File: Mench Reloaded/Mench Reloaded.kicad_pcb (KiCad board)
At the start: 2 copper layers, 100 x 100 mm, 55 parts, among them IC1 DS1813, J1 XBUS_265, J10 Int Sel 1, J11 VIA1 Port A, J12 VIA1 Port B, J2 TGx, J3 RAM CSB select, J4 P4x, J5 P5x, J6 P6x, J7 FTDI serial, J8 EEPROM R/W, J9 DC Power, SW1 SW_Push, U1 W65C265SxQ, U2 68c128 SRAM, U3 28C256, U4 LM1117 TO-252-3, U5 74HC00, U6 W65C22SxP, Y1 32.768 kHz, Y2 3.6864 mHz

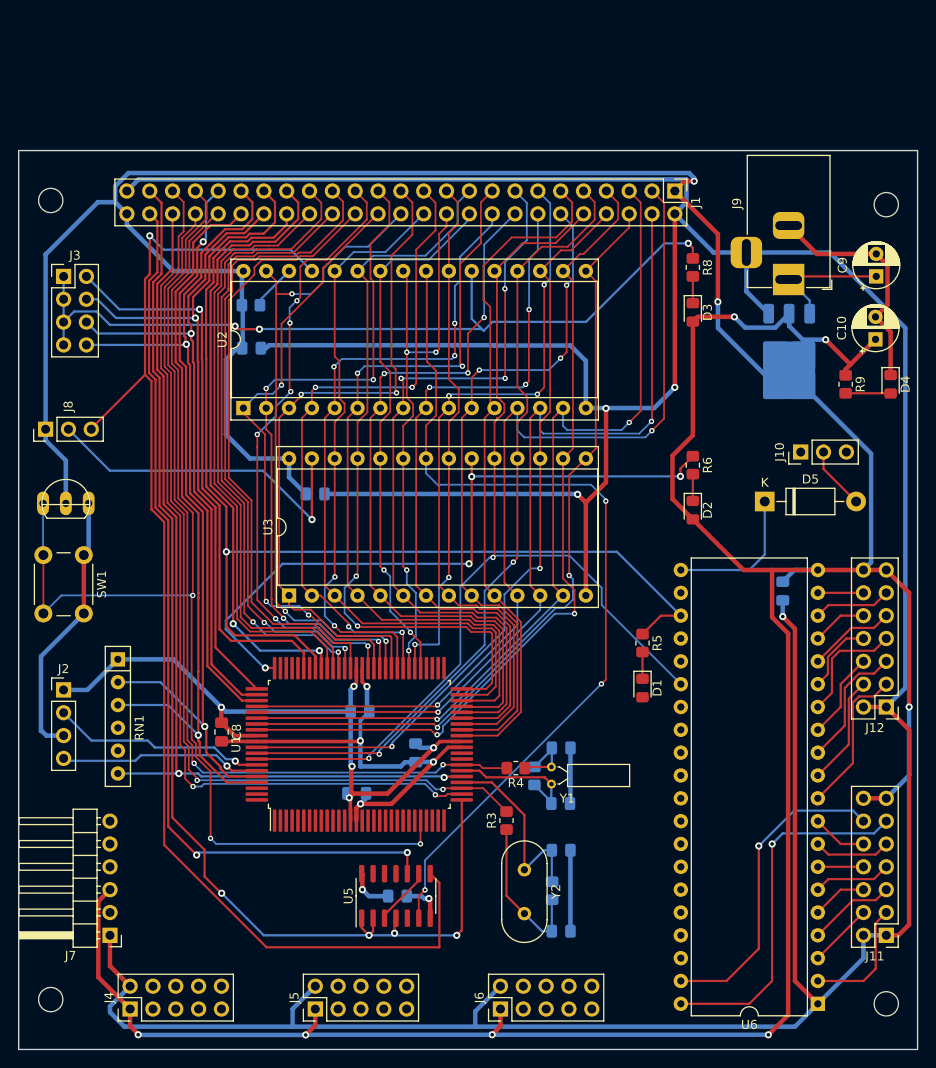
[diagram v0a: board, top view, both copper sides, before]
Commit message: Routed traces for the 65c22.
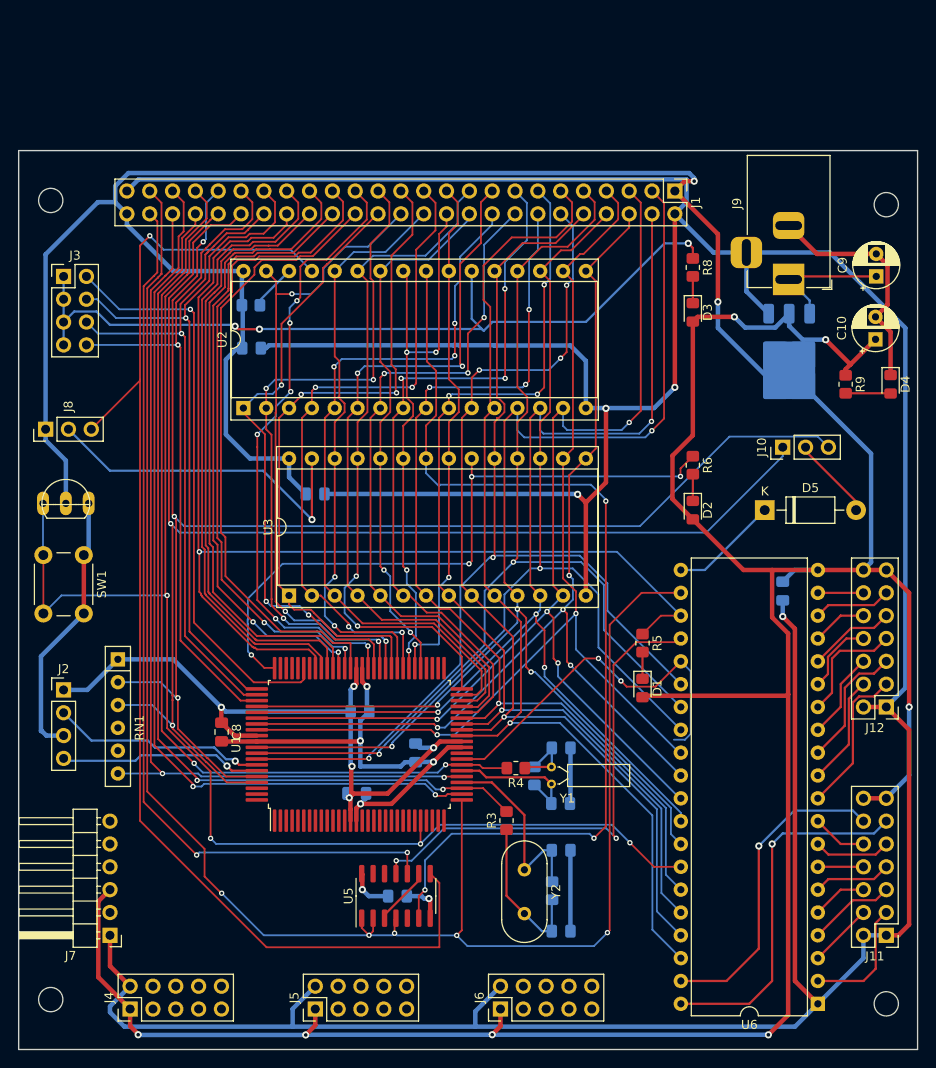
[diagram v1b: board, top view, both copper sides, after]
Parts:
- moved J10 2.07 mm to (140.0, 78.0)
- moved D5 0.96 mm to (138.0, 85.0)
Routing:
- net NMIB: track 84.0 -> 158.4 mm, vias 2 -> 3
- net IRQB: track 83.5 -> 153.9 mm, vias 1 -> 2
- net WEB: track 131.9 -> 194.0 mm, vias 4 -> 5
- net A5B: track 0.00 -> 56.0 mm, vias 0 -> 2
- net PHI2: track 100.2 -> 142.8 mm, vias 2 -> 4
- net a0: track 75.8 -> 113.1 mm, vias 0 -> 1
- net a1: track 76.3 -> 110.6 mm, vias 3 -> 4
- net d0: track 103.9 -> 137.9 mm, vias 2 -> 4
- net a2: track 81.1 -> 112.1 mm, vias 3 -> 4
- net d1: track 98.3 -> 128.0 mm, vias 2 -> 4
- net RESB: track 129.5 -> 159.0 mm, vias 3 -> 4
- net a3: track 80.1 -> 108.8 mm, vias 3 -> 4
- net d6: track 89.4 -> 117.6 mm
- net d2: track 98.3 -> 125.3 mm, vias 2 -> 4
- net d5: track 86.4 -> 113.0 mm
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
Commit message: Completed all traces. Added a Zif socket footprint to ensure one will fit. Added a solder jumper for RAM options.
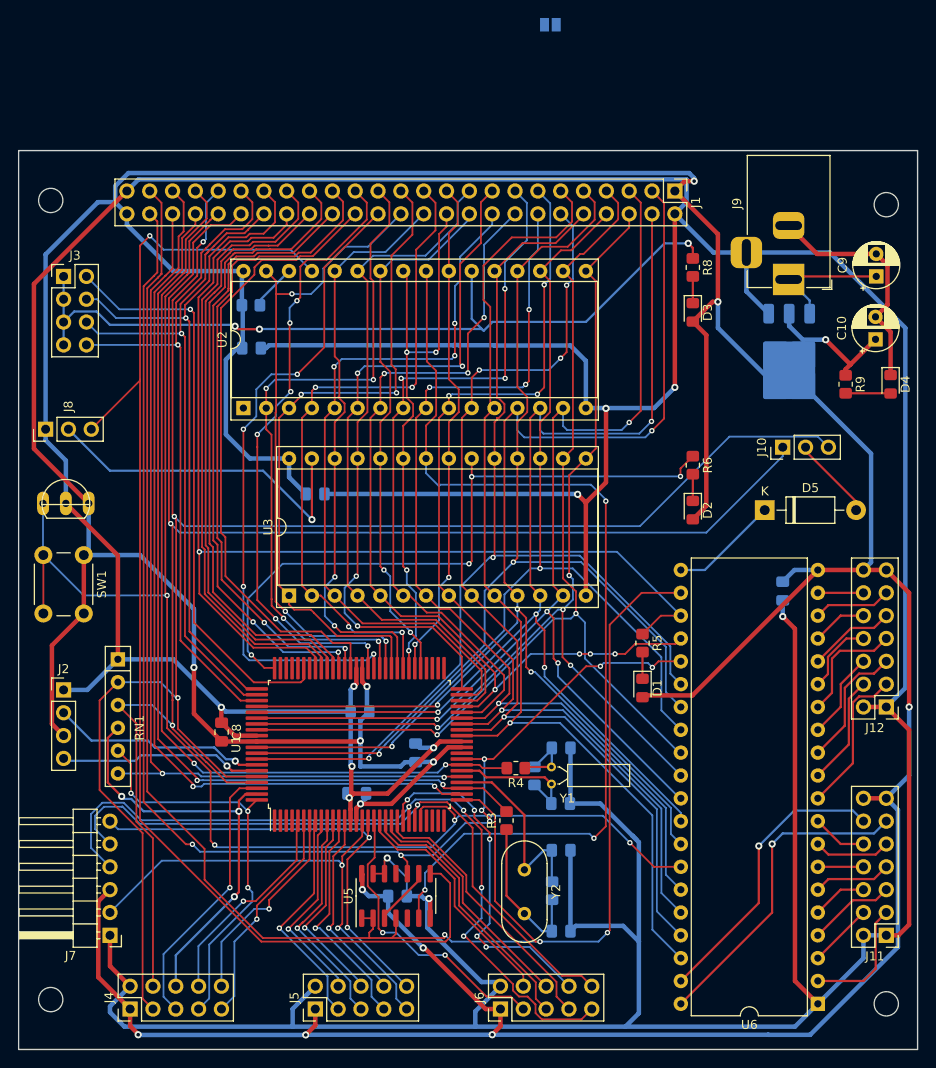
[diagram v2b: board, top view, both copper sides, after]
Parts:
- added JP1: 68c256 Jumper, Jumper:SolderJumper-2_P1.3mm_Open_Pad1.0x1.5mm, B.Cu at (114.2, 31.0)
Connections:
- U2 pad 1: a17 -> unconnected-(U2-NC-Pad1)
- U5 pad 11: A5B -> unconnected-(U5-Pad11)
- U5 pad 12: a5 -> GND
- U5 pad 13: a5 -> GND
- U6 pad 24: A5B -> a5
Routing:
- net GND: track 593.7 -> 726.1 mm, vias 9 -> 11
- net RXD3: track 0.00 -> 87.8 mm, vias 0 -> 4
- net TXD3: track 0.00 -> 75.6 mm, vias 0 -> 1
- net A5B: track 56.0 -> 0.00 mm, vias 2 -> 0
- net DTRB3: track 0.00 -> 53.9 mm, vias 0 -> 2
- net DSRB3: track 0.00 -> 51.8 mm, vias 0 -> 2
- net FA15: track 0.00 -> 48.3 mm, vias 0 -> 3
- net AMS: track 0.00 -> 45.5 mm, vias 0 -> 3
- net NMIB: track 158.4 -> 198.0 mm
- net TXD2: track 0.00 -> 39.1 mm, vias 0 -> 5
- net IRQB: track 153.9 -> 186.8 mm
- net RXD0: track 0.00 -> 32.7 mm, vias 0 -> 2
- net PIIB: track 0.00 -> 30.6 mm, vias 0 -> 1
- net RXD2: track 0.00 -> 30.6 mm
- net RXD1: track 0.00 -> 30.2 mm
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
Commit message: Added power selector header (ftdi vs battery). Added 128kB vs 256kB RAM selector. Added pull up for RESB and DS1813. Reworked traces at top of the board using streets and avenues.
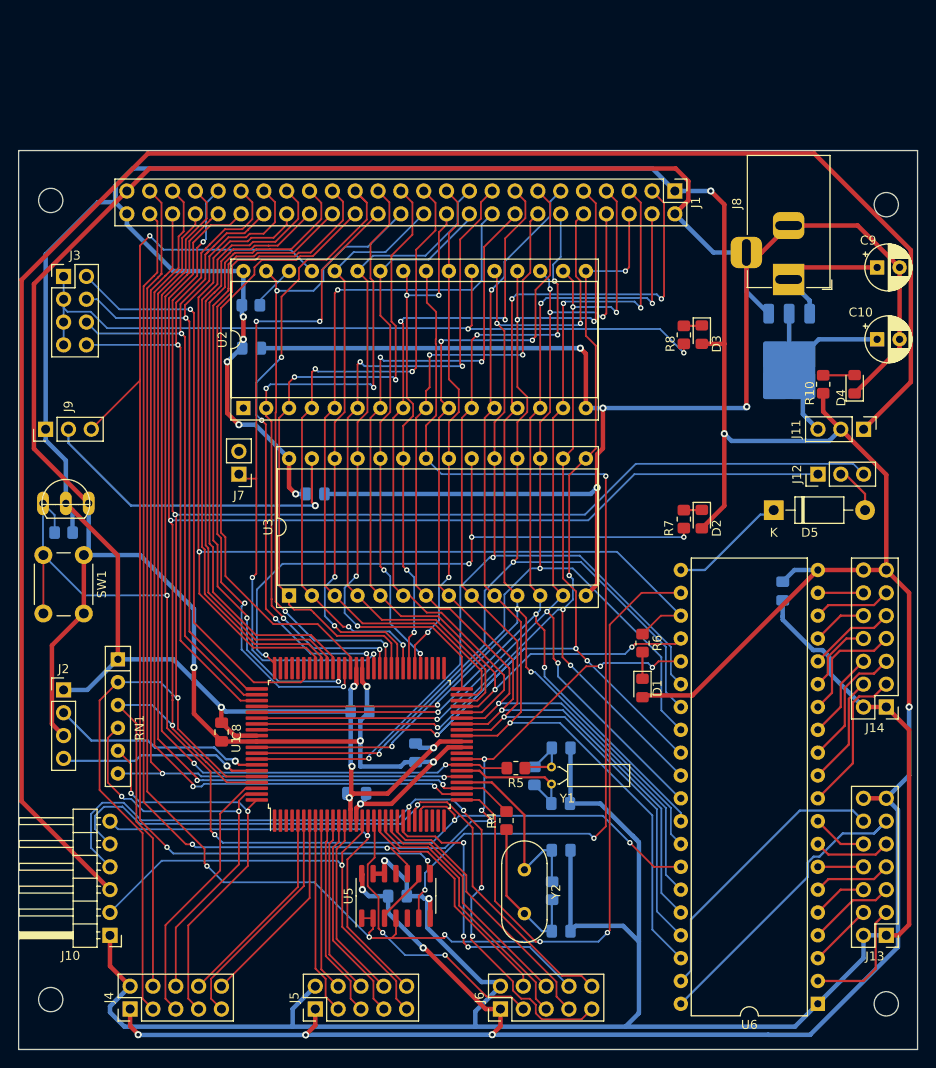
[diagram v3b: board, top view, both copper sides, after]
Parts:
- removed JP1: 68c256 Jumper, Jumper:SolderJumper-2_P1.3mm_Open_Pad1.0x1.5mm
- added J11: Power Sel, Connector_PinHeader_2.54mm:PinHeader_1x03_P2.54mm_Vertical, F.Cu at (149.0, 76.0)
- added J7: 68c256 Sel, Connector_PinHeader_2.54mm:PinHeader_1x02_P2.54mm_Vertical, F.Cu at (79.5, 81.0)
- added R1: 3K, Resistor_SMD:R_0805_2012Metric_Pad1.20x1.40mm_HandSolder, B.Cu at (60.0, 87.5)
- D1, D2, D3: value green -> LED
- J12: renamed from J10; value Int Sel 1 -> Int Sel
- moved R8 7.57 mm to (129.0, 65.5), turned to 90 degrees
- moved R7 6.08 mm to (129.0, 86.0), turned to 90 degrees
- moved J12 4.94 mm to (143.9, 81.0)
- moved D4 4.00 mm to (148.0, 71.0), turned to 90 degrees
- moved D3 2.67 mm to (131.0, 65.5)
- moved R10 2.50 mm to (144.5, 71.0), turned to 90 degrees
- moved D2 1.41 mm to (131.0, 86.0)
- moved C9 1.00 mm to (150.5, 58.0), turned to 0 degrees
- moved D5 1.00 mm to (139.0, 85.0)
- moved C10 0.18 mm to (150.5, 66.0), turned to 0 degrees
- renumbered J7 to J10, J11 to J13, J12 to J14, J9 to J8, J8 to J9, R9 to R10, R1 to R2, R2 to R3, R3 to R4, R4 to R5, R5 to R6, R6 to R7, R7 to R9
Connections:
- C10 pad 1: +5V -> Net-(J11-Pin_3)
- J10 pad 3: +5V -> Net-(J10-Pin_3)
- U4 pad 2: +5V -> Net-(J11-Pin_3)
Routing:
- net Net-(J10-Pin_3): track 0.00 -> 203.2 mm
- net GND: track 726.1 -> 648.5 mm
- net +5V: track 570.7 -> 544.4 mm, vias 14 -> 18
- net Net-(J11-Pin_3): track 0.00 -> 20.9 mm
- net d4: track 113.6 -> 132.1 mm, vias 2 -> 5
- net MEMWEB: track 141.8 -> 128.3 mm, vias 1 -> 3
- net d7: track 115.2 -> 124.7 mm, vias 2 -> 4
- net d6: track 117.6 -> 126.9 mm, vias 2 -> 4
- net d5: track 113.0 -> 120.6 mm, vias 2 -> 5
- net a15: track 78.5 -> 72.2 mm
- net a11: track 65.1 -> 58.8 mm
- net TXD2: track 39.1 -> 33.3 mm, vias 5 -> 3
- net a20: track 73.1 -> 78.4 mm
- net MEMCS1B: track 91.4 -> 86.3 mm, vias 3 -> 2
- net a0: track 113.1 -> 108.5 mm, vias 1 -> 2
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
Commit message: Moved EEPROM North to create more space for traces. Reworked all traces from CPU to fix rats nest wiring. Added LED to csb2 to allow for debugging when internal bus is used. Added to list of signal net classes to make consistant data traces.
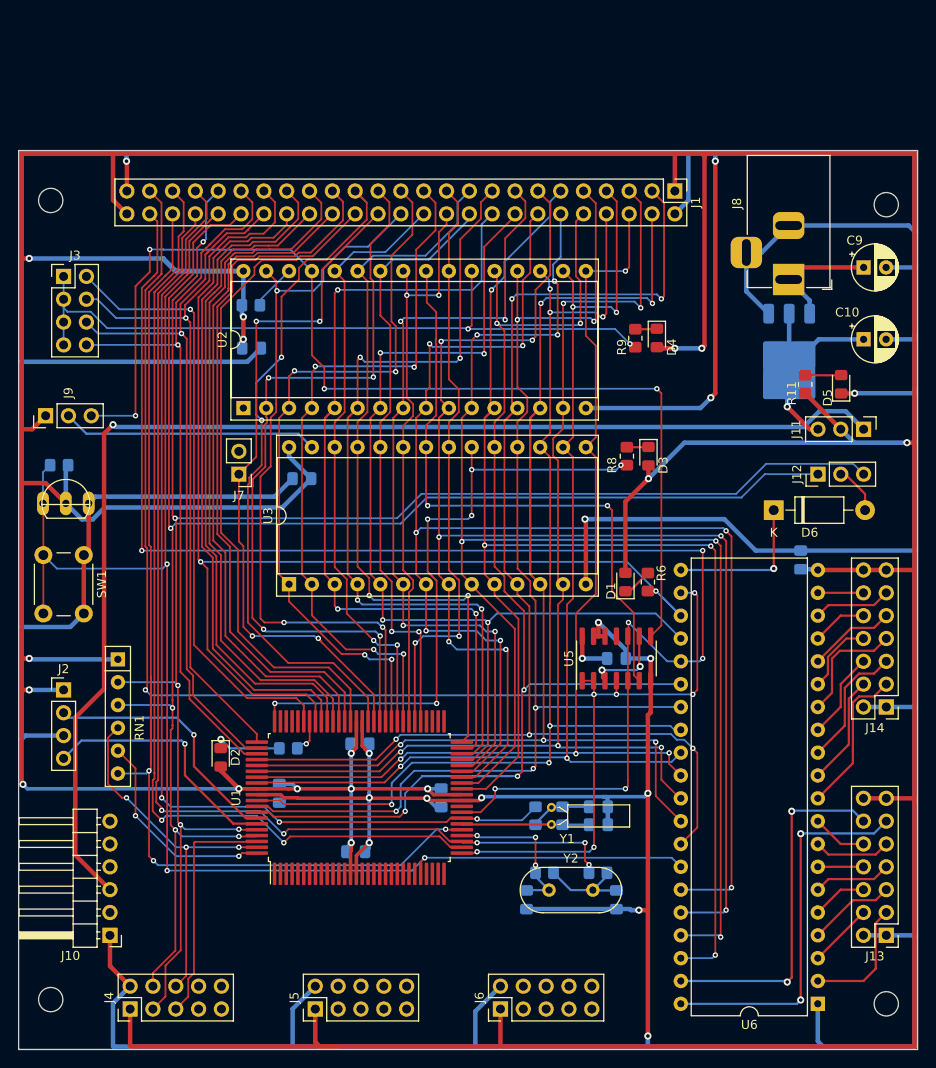
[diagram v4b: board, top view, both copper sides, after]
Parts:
- added D2: LED, LED_SMD:LED_0805_2012Metric_Pad1.15x1.40mm_HandSolder, F.Cu at (77.5, 112.5)
- added R7: 3K, Resistor_SMD:R_0805_2012Metric_Pad1.20x1.40mm_HandSolder, B.Cu at (85.0, 111.5)
- C8, R4, R5: moved to B.Cu
- moved U5 36.0 mm to (121.5, 101.5)
- moved C13 36.0 mm to (121.5, 101.5)
- moved D1 11.9 mm to (122.5, 93.0), turned to 90 degrees
- moved R4 11.7 mm to (119.4, 125.3), turned to 180 degrees
- moved R8 9.44 mm to (122.7, 79.0)
- moved C8 9.37 mm to (84.0, 116.5)
- moved D3 9.18 mm to (125.1, 79.0)
- moved C3 7.75 mm to (119.5, 118.0)
- moved R1 7.52 mm to (59.5, 80.0)
- moved C4 7.08 mm to (121.5, 128.3), turned to -90 degrees
- moved R6 6.81 mm to (125.0, 93.0), turned to 90 degrees
- moved C2 6.72 mm to (111.5, 128.3), turned to -90 degrees
- moved C5 6.49 mm to (92.5, 123.0)
- moved U1 5.92 mm to (92.9, 117.0)
- moved C7 5.75 mm to (102.0, 117.0)
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- renumbered D2 to D3, D3 to D4, D4 to D5, D5 to D6, R9 to R10, R10 to R11, R7 to R8, R8 to R9
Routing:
- net +5V: track 544.4 -> 668.1 mm, vias 18 -> 17
- net GND: track 648.5 -> 755.5 mm, vias 11 -> 15
- net RXD3: track 87.1 -> 0.00 mm, vias 4 -> 0
- net TXD3: track 75.6 -> 0.00 mm, vias 1 -> 0
- net Net-(J10-Pin_3): track 203.2 -> 140.2 mm, vias 0 -> 1
- net a3: track 109.7 -> 165.2 mm, vias 3 -> 7
- net DTRB3: track 53.2 -> 0.00 mm, vias 1 -> 0
- net a2: track 113.8 -> 166.9 mm, vias 3 -> 7
- net DSRB3: track 51.4 -> 0.00 mm, vias 1 -> 0
- net a1: track 111.0 -> 156.7 mm, vias 4 -> 6
- net a0: track 108.5 -> 152.6 mm, vias 2 -> 4
- net MEMOEB: track 109.6 -> 69.4 mm, vias 3 -> 2
- net TXD2: track 33.3 -> 0.00 mm, vias 3 -> 0
- net RXD0: track 32.7 -> 0.00 mm, vias 2 -> 0
- net WEB: track 198.3 -> 167.6 mm, vias 5 -> 7
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
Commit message: Updated README and added an image of the board.
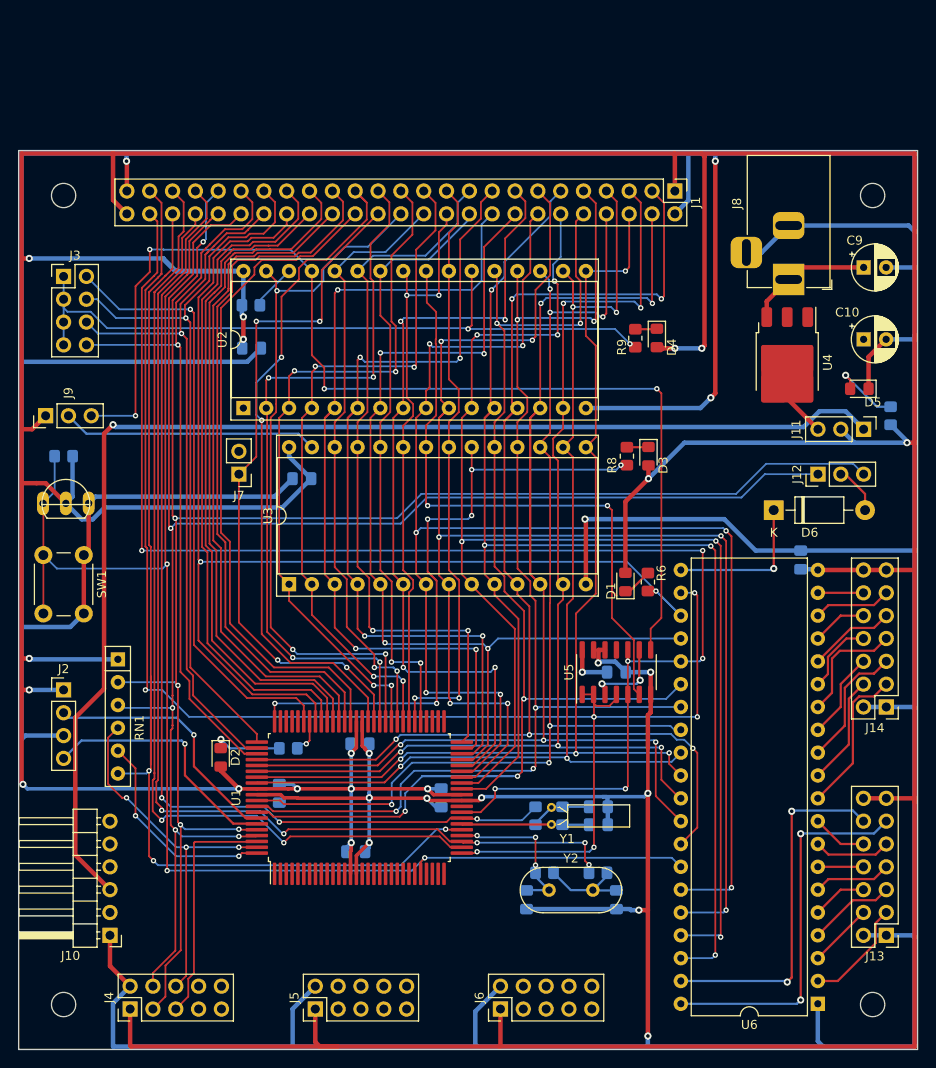
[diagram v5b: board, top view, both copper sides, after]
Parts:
- R11: moved to B.Cu
- U4: moved to F.Cu
- moved R11 10.1 mm to (152.0, 74.5)
- moved D5 2.09 mm to (148.5, 71.5), turned to 180 degrees
- moved MH3 1.83 mm to (150.0, 50.0)
- moved MH2 1.53 mm to (60.0, 140.0)
- moved MH1 1.53 mm to (60.0, 50.0)
- moved C13 1.53 mm to (121.5, 103.0)
- moved U5 1.53 mm to (121.5, 103.0)
- moved MH4 1.52 mm to (150.0, 140.0)
- moved R1 1.12 mm to (60.0, 79.0)
- moved U4 0.44 mm to (140.5, 68.6)
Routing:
- net GND: track 755.5 -> 741.5 mm, vias 15 -> 14
- net Net-(J11-Pin_3): track 21.2 -> 7.59 mm, vias 1 -> 0
- net MEMOEB: track 69.4 -> 75.7 mm
- net PHI2: track 161.6 -> 156.8 mm
- net Net-(D5-A): track 4.01 -> 8.16 mm, vias 0 -> 1
- net WEB: track 167.6 -> 171.7 mm, vias 7 -> 6
- net a16: track 86.0 -> 82.9 mm
- net a15: track 82.6 -> 80.0 mm
- net a12: track 80.4 -> 78.6 mm
- net a14: track 80.9 -> 79.1 mm
- net +5V: track 668.1 -> 666.4 mm
- net Net-(J13-Pin_3): track 13.7 -> 12.1 mm
- net MEMWEB: track 122.0 -> 123.5 mm
- net a18: track 77.0 -> 75.4 mm
- net a5: track 111.3 -> 109.9 mm
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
